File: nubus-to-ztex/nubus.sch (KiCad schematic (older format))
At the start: 53 parts, among them J4 85003-0567 (DIN 41612C 3x32 p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, U1 74LVT125PW,118, U13 SN74CB3T3245PWR, U14 SN74CB3T3245PWR, U15 SN74CB3T3245PWR, U2 74LVT125PW,118, U3 74LVT125PW,118, U5 74LVT245BPW,118, U6 74LVT245BPW,118, U7 74LVT245BPW,118, U8 74LVT245BPW,118

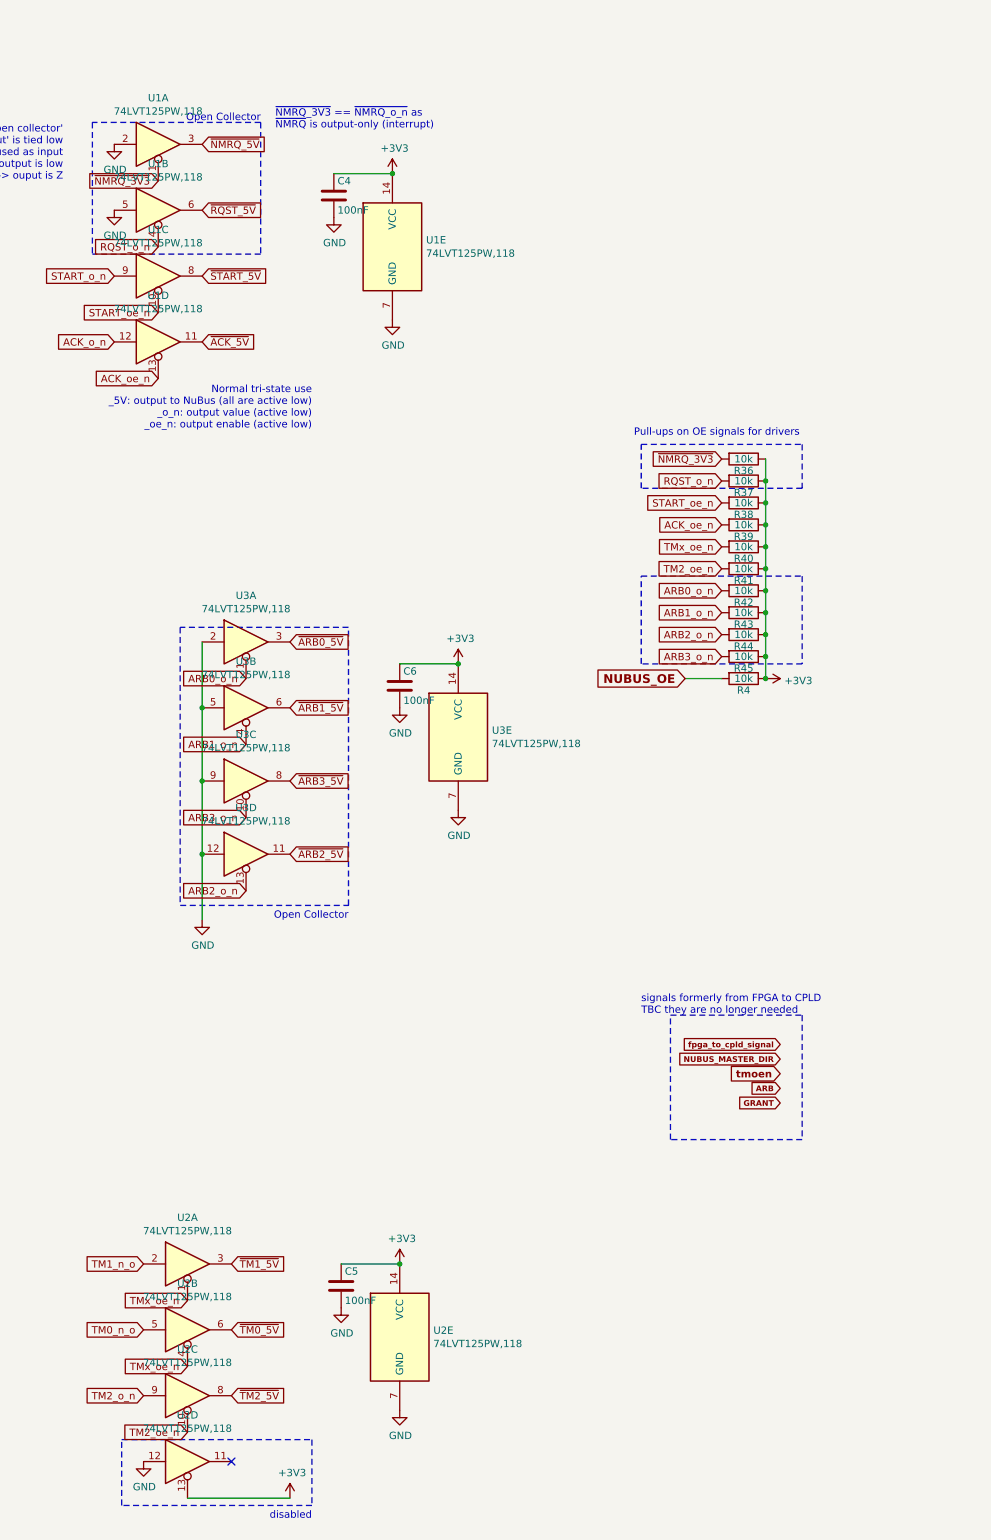
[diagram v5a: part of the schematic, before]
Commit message: even more JLCPCB BoM optimization
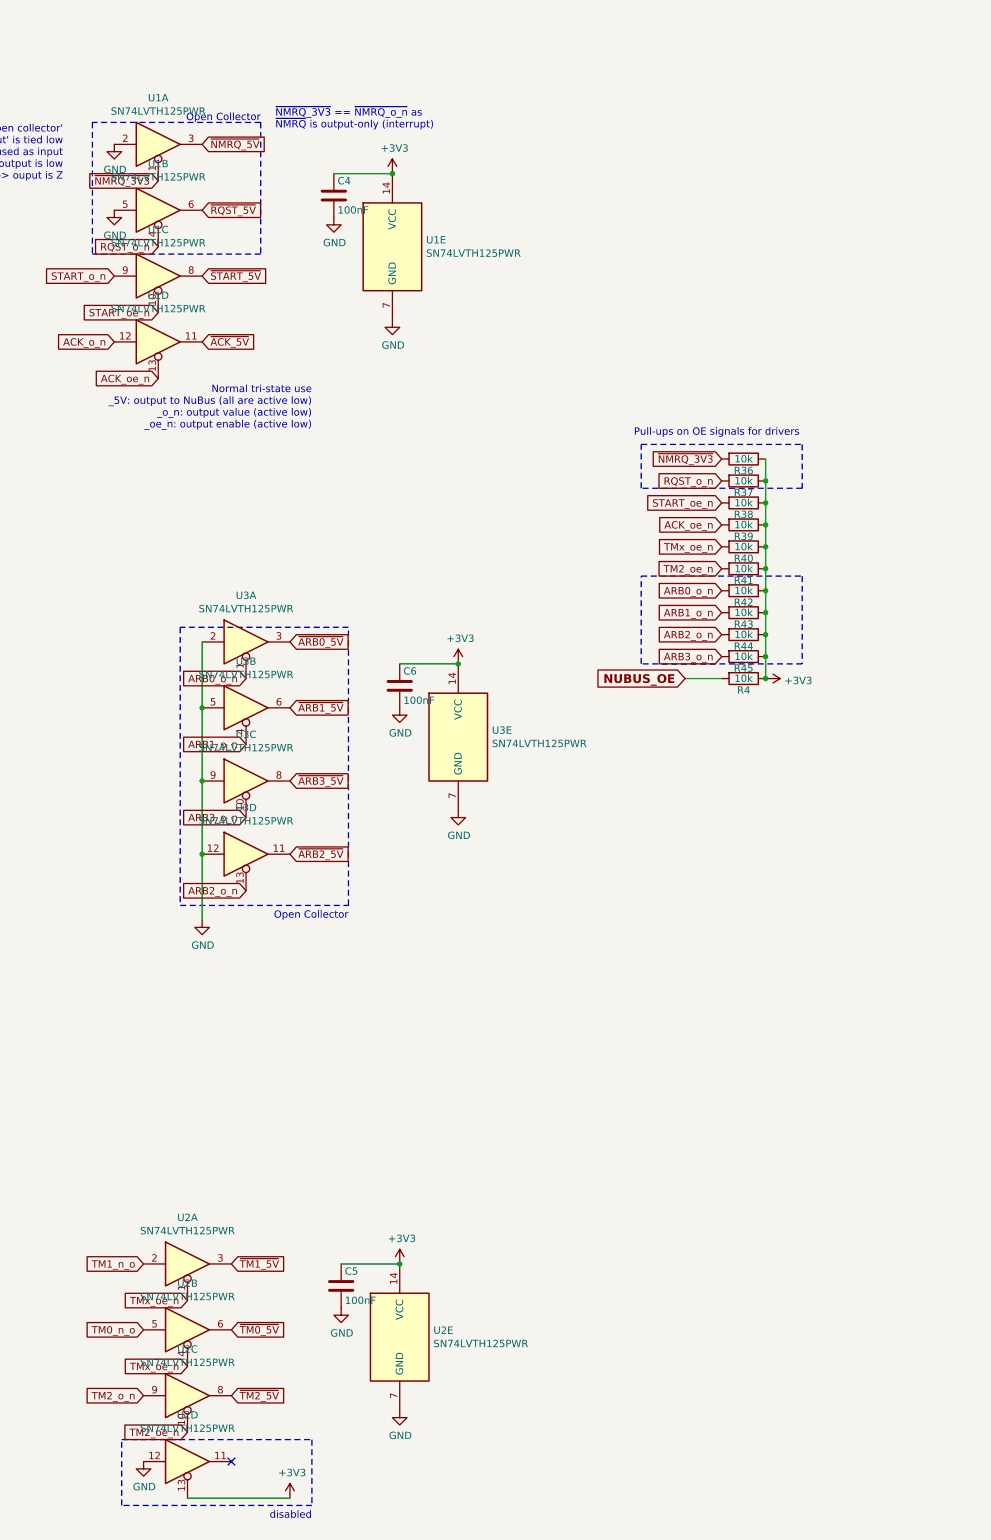
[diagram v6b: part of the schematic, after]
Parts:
- U1, U2, U3: value 74LVT125PW,118 -> SN74LVTH125PWR; MPN 74LVT125PW,118 -> SN74LVTH125PWR; URL https://www.lcsc.com/product-detail/Buffer-Driver-Transceiver_Nexperia-74LVT125PW-118_C6108.html -> https://www.lcsc.com/product-detail/Buffer-Driver-Transceiver_Texas-Instruments-SN74LVTH125PWR_C7042.html
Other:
- note removed: "signals formerly from FPGA to CPLD\nTBC they are no longer needed"

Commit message: minor changes in BoM
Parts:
- added C16, C29, C31, C32: 1uF, Capacitor_SMD:C_0603_1608Metric, symbol Device:C
- U5, U6, U7, U8: value 74LVT245BPW,118 -> SN74LVT245BPWR; MPN SN74LVT245BPWR -> SN74LVTH245APWR; URL https://lcsc.com/product-detail/Receivers-Transceivers_Texa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 -> https://www.lcsc.com/product-detail/Buffer-Driver-Transceiv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
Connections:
- net +3V3: now also C16.1, C29.1, C31.1, C32.1
- net GND: now also C16.2, C29.2, C31.2, C32.2
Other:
- note added: "Notes on MPN:\n74LVT and 74LVTH differs by the 'bus hold' feature on the'H' variant\n(see <https://assets.nexperia.com/documents/white-paper/Nexperia_document_whitepaper_FloatingInputs_Logic_BusHold_201909.pdf>)\nBoth should work, 'H' variant seems more available @JLCPCB"
- note added: "close to U13"
- note added: "close to tm0/1 leds"
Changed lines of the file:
@@
 P 17350 3450
 F 0 "U8" H 17350 4428 50  0000 C CNN
-F 1 "74LVT245BPW,118" H 17350 4337 50  0000 C CNN
+F 1 "SN74LVT245BPWR" H 17350 4337 50  0000 C CNN
 F 2 "For_SeeedStudio:TSSOP-20_4.4x6.5mm_P0.65mm_ForSeeedStudio" H 17350 3450 50  0001 C CNN
 F 3 "http://www.ti.com/lit/gpn/sn74LS245" H 17350 3450 50  0001 C CNN
@@
 F 5 "74LVT245BPW,118" H 17350 3450 50  0001 C CNN "MPN - ALT"
 F 6 "https://www.digikey.fr/fr/products/detail/nexperia-usa-inc/74LVT245BPW-118/1231957" H 17350 3450 50  0001 C CNN "URL - ALT"
-F 7 "SN74LVT245BPWR" H 17350 3450 50  0001 C CNN "MPN"
-F 8 "https://lcsc.com/product-detail/Receivers-Transceivers_Texas-Instruments-SN74LVT245BPWR_C74214.html" H 17350 3450 50  0001 C CNN "URL"
+F 7 "SN74LVTH245APWR" H 17350 3450 50  0001 C CNN "MPN"
+F 8 "https://www.lcsc.com/product-detail/Buffer-Driver-Transceiver_Texas-Instruments-SN74LVTH245APWR_C2652121.html" H 17350 3450 50  0001 C CNN "URL"
 	1    17350 3450
 	-1   0    0    -1
@@
 P 15350 3450
 F 0 "U7" H 15350 4428 50  0000 C CNN
-F 1 "74LVT245BPW,118" H 15350 4337 50  0000 C CNN
+F 1 "SN74LVT245BPWR" H 15350 4337 50  0000 C CNN
 F 2 "For_SeeedStudio:TSSOP-20_4.4x6.5mm_P0.65mm_ForSeeedStudio" H 15350 3450 50  0001 C CNN
 F 3 "http://www.ti.com/lit/gpn/sn74LS245" H 15350 3450 50  0001 C CNN
@@
 F 5 "https://eu.mouser.com/ProductDetail/?qs=me8TqzrmIYVnC5%252BK4SaiTg%3D%3D" H 15350 3450 50  0001 C CNN "URL - ALT - mouser"
 F 6 "https://www.digikey.fr/fr/products/detail/nexperia-usa-inc/74LVT245BPW-118/1231957" H 15350 3450 50  0001 C CNN "URL - ALT"
-F 7 "SN74LVT245BPWR" H 15350 3450 50  0001 C CNN "MPN"
-F 8 "https://lcsc.com/product-detail/Receivers-Transceivers_Texas-Instruments-SN74LVT245BPWR_C74214.html" H 15350 3450 50  0001 C CNN "URL"
+F 7 "SN74LVTH245APWR" H 15350 3450 50  0001 C CNN "MPN"
+F 8 "https://www.lcsc.com/product-detail/Buffer-Driver-Transceiver_Texas-Instruments-SN74LVTH245APWR_C2652121.html" H 15350 3450 50  0001 C CNN "URL"
 	1    15350 3450
 	-1   0    0    -1
@@
 P 13300 3450
 F 0 "U6" H 13300 4428 50  0000 C CNN
-F 1 "74LVT245BPW,118" H 13300 4337 50  0000 C CNN
+F 1 "SN74LVT245BPWR" H 13300 4337 50  0000 C CNN
 F 2 "For_SeeedStudio:TSSOP-20_4.4x6.5mm_P0.65mm_ForSeeedStudio" H 13300 3450 50  0001 C CNN
 F 3 "http://www.ti.com/lit/gpn/sn74LS245" H 13300 3450 50  0001 C CNN
@@
 F 5 "https://eu.mouser.com/ProductDetail/?qs=me8TqzrmIYVnC5%252BK4SaiTg%3D%3D" H 13300 3450 50  0001 C CNN "URL - ALT - mouser"
 F 6 "https://www.digikey.fr/fr/products/detail/nexperia-usa-inc/74LVT245BPW-118/1231957" H 13300 3450 50  0001 C CNN "URL - ALT"
-F 7 "SN74LVT245BPWR" H 13300 3450 50  0001 C CNN "MPN"
-F 8 "https://lcsc.com/product-detail/Receivers-Transceivers_Texas-Instruments-SN74LVT245BPWR_C74214.html" H 13300 3450 50  0001 C CNN "URL"
+F 7 "SN74LVTH245APWR" H 13300 3450 50  0001 C CNN "MPN"
+F 8 "https://www.lcsc.com/product-detail/Buffer-Driver-Transceiver_Texas-Instruments-SN74LVTH245APWR_C2652121.html" H 13300 3450 50  0001 C CNN "URL"
 	1    13300 3450
 	-1   0    0    -1
@@
 P 11250 3450
 F 0 "U5" H 11250 4428 50  0000 C CNN
-F 1 "74LVT245BPW,118" H 11250 4337 50  0000 C CNN
+F 1 "SN74LVT245BPWR" H 11250 4337 50  0000 C CNN
 F 2 "For_SeeedStudio:TSSOP-20_4.4x6.5mm_P0.65mm_ForSeeedStudio" H 11250 3450 50  0001 C CNN
 F 3 "http://www.ti.com/lit/gpn/sn74LS245" H 11250 3450 50  0001 C CNN
@@
 F 8 "https://assets.nexperia.com/documents/package-information/SOT360-1.pdf" H 11250 3450 50  0001 C CNN "Package Drawings"
 F 9 "https://www.digikey.fr/fr/products/detail/nexperia-usa-inc/74LVT245BPW-118/1231957" H 11250 3450 50  0001 C CNN "URL - ALT"
-F 10 "SN74LVT245BPWR" H 11250 3450 50  0001 C CNN "MPN"
-F 11 "https://lcsc.com/product-detail/Receivers-Transceivers_Texas-Instruments-SN74LVT245BPWR_C74214.html" H 11250 3450 50  0001 C CNN "URL"
+F 10 "SN74LVTH245APWR" H 11250 3450 50  0001 C CNN "MPN"
+F 11 "https://www.lcsc.com/product-detail/Buffer-Driver-Transceiver_Texas-Instruments-SN74LVTH245APWR_C2652121.html" H 11250 3450 50  0001 C CNN "URL"
 	1    11250 3450
 	-1   0    0    -1
@@
 	1    0    0    -1
 $EndComp
+Text Notes 5200 2000 0    50   Italic 0
+Notes on MPN:\n74LVT and 74LVTH differs by the 'bus hold' feature on the'H' variant\n(see <https://assets.nexperia.com/documents/white-paper/Nexperia_document_whitepaper_FloatingInputs_Logic_BusHold_201909.pdf>)\nBoth should work, 'H' variant seems more available @JLCPCB
+$Comp
+L Device:C C16
+U 1 1 649F6D34
+P 16350 2525
+F 0 "C16" H 16375 2625 50  0000 L CNN
+F 1 "1uF" H 16375 2425 50  0000 L CNN
+F 2 "Capacitor_SMD:C_0603_1608Metric" H 16388 2375 50  0001 C CNN
+F 3 "" H 16350 2525 50  0000 C CNN
+F 4 "CL10A105KB8NNNC" H 16350 2525 50  0001 C CNN "MPN"
+	1    16350 2525
+	1    0    0    -1
+$EndComp
+$Comp
+L power:GND #PWR0141
+U 1 1 649F924E
+P 16350 2675
+F 0 "#PWR0141" H 16350 2425 50  0001 C CNN
+F 1 "GND" H 16355 2502 50  0000 C CNN
+F 2 "" H 16350 2675 50  0001 C CNN
+F 3 "" H 16350 2675 50  0001 C CNN
+	1    16350 2675
+	1    0    0    -1
+$EndComp
+$Comp
+L power:+3V3 #PWR0149
+U 1 1 649F97D4
+P 16350 2375
+F 0 "#PWR0149" H 16350 2225 50  0001 C CNN
+F 1 "+3V3" H 16365 2548 50  0000 C CNN
+F 2 "" H 16350 2375 50  0001 C CNN
+F 3 "" H 16350 2375 50  0001 C CNN
+	1    16350 2375
+	1    0    0    -1
+$EndComp
+$Comp
+L Device:C C29
+U 1 1 649FF55F
+P 12250 2550
+F 0 "C29" H 12275 2650 50  0000 L CNN
+F 1 "1uF" H 12275 2450 50  0000 L CNN
+F 2 "Capacitor_SMD:C_0603_1608Metric" H 12288 2400 50  0001 C CNN
+F 3 "" H 12250 2550 50  0000 C CNN
+F 4 "CL10A105KB8NNNC" H 12250 2550 50  0001 C CNN "MPN"
+	1    12250 2550
+	1    0    0    -1
+$EndComp
+$Comp
+L power:GND #PWR0150
+U 1 1 649FF565
+P 12250 2700
+F 0 "#PWR0150" H 12250 2450 50  0001 C CNN
+F 1 "GND" H 12255 2527 50  0000 C CNN
+F 2 "" H 12250 2700 50  0001 C CNN
+F 3 "" H 12250 2700 50  0001 C CNN
+	1    12250 2700
+	1    0    0    -1
+$EndComp
+$Comp
+L power:+3V3 #PWR0153
+U 1 1 649FF56B
+P 12250 2400
+F 0 "#PWR0153" H 12250 2250 50  0001 C CNN
+F 1 "+3V3" H 12265 2573 50  0000 C CNN
+F 2 "" H 12250 2400 50  0001 C CNN
+F 3 "" H 12250 2400 50  0001 C CNN
+	1    12250 2400
+	1    0    0    -1
+$EndComp
+$Comp
+L Device:C C31
+U 1 1 64A331D7
+P 11775 9275
+F 0 "C31" H 11800 9375 50  0000 L CNN
+F 1 "1uF" H 11800 9175 50  0000 L CNN
+F 2 "Capacitor_SMD:C_0603_1608Metric" H 11813 9125 50  0001 C CNN
+F 3 "" H 11775 9275 50  0000 C CNN
+F 4 "CL10A105KB8NNNC" H 11775 9275 50  0001 C CNN "MPN"
+	1    11775 9275
+	1    0    0    -1
+$EndComp
+$Comp
+L power:GND #PWR0154
+U 1 1 64A331DD
+P 11775 9425
+F 0 "#PWR0154" H 11775 9175 50  0001 C CNN
+F 1 "GND" H 11780 9252 50  0000 C CNN
+F 2 "" H 11775 9425 50  0001 C CNN
+F 3 "" H 11775 9425 50  0001 C CNN
+	1    11775 9425
+	1    0    0    -1
+$EndComp
+$Comp
+L power:+3V3 #PWR0155
+U 1 1 64A331E3
+P 11775 9125
+F 0 "#PWR0155" H 11775 8975 50  0001 C CNN
+F 1 "+3V3" H 11790 9298 50  0000 C CNN
+F 2 "" H 11775 9125 50  0001 C CNN
+F 3 "" H 11775 9125 50  0001 C CNN
+	1    11775 9125
+	1    0    0    -1
+$EndComp
+$Comp
+L Device:C C32
+U 1 1 64A8746F
+P 13200 13350
+F 0 "C32" H 13225 13450 50  0000 L CNN
+F 1 "1uF" H 13225 13250 50  0000 L CNN
+F 2 "Capacitor_SMD:C_0603_1608Metric" H 13238 13200 50  0001 C CNN
+F 3 "" H 13200 13350 50  0000 C CNN
+F 4 "CL10A105KB8NNNC" H 13200 13350 50  0001 C CNN "MPN"
+	1    13200 13350
+	1    0    0    -1
+$EndComp
+$Comp
+L power:GND #PWR0156
+U 1 1 64A87475
+P 13200 13500
+F 0 "#PWR0156" H 13200 13250 50  0001 C CNN
+F 1 "GND" H 13205 13327 50  0000 C CNN
+F 2 "" H 13200 13500 50  0001 C CNN
+F 3 "" H 13200 13500 50  0001 C CNN
+	1    13200 13500
+	1    0    0    -1
+$EndComp
+$Comp
+L power:+3V3 #PWR0157
+U 1 1 64A8747B
+P 13200 13200
+F 0 "#PWR0157" H 13200 13050 50  0001 C CNN
+F 1 "+3V3" H 13215 13373 50  0000 C CNN
+F 2 "" H 13200 13200 50  0001 C CNN
+F 3 "" H 13200 13200 50  0001 C CNN
+	1    13200 13200
+	1    0    0    -1
+$EndComp
+Text Notes 11575 9650 1    50   Italic 0
+close to tm0/1 leds
+Text Notes 13075 13600 1    50   Italic 0
+close to U13
 $EndSCHEMATC
